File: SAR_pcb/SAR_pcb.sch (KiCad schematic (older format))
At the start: 47 parts, among them J1 Conn_Coaxial_Power, J10 Conn_Coaxial, J12 Conn_01x02, J13 Conn_01x02, J14 Conn_01x02, J15 Conn_01x02, J16 Conn_01x02, J17 Conn_01x02, J18 Conn_01x02, J19 Conn_01x02, J2 Conn_Coaxial_Power, J20 Conn_01x02, J21 Conn_01x02, J3 Conn_Coaxial_Power, J4 Conn_Coaxial_Power, J5 Conn_Coaxial_Power, J6 Conn_01x02_Male, J7 Conn_01x02_Male, J8 Conn_01x02_Male, J9 Conn_Coaxial, U2 10B_SAR

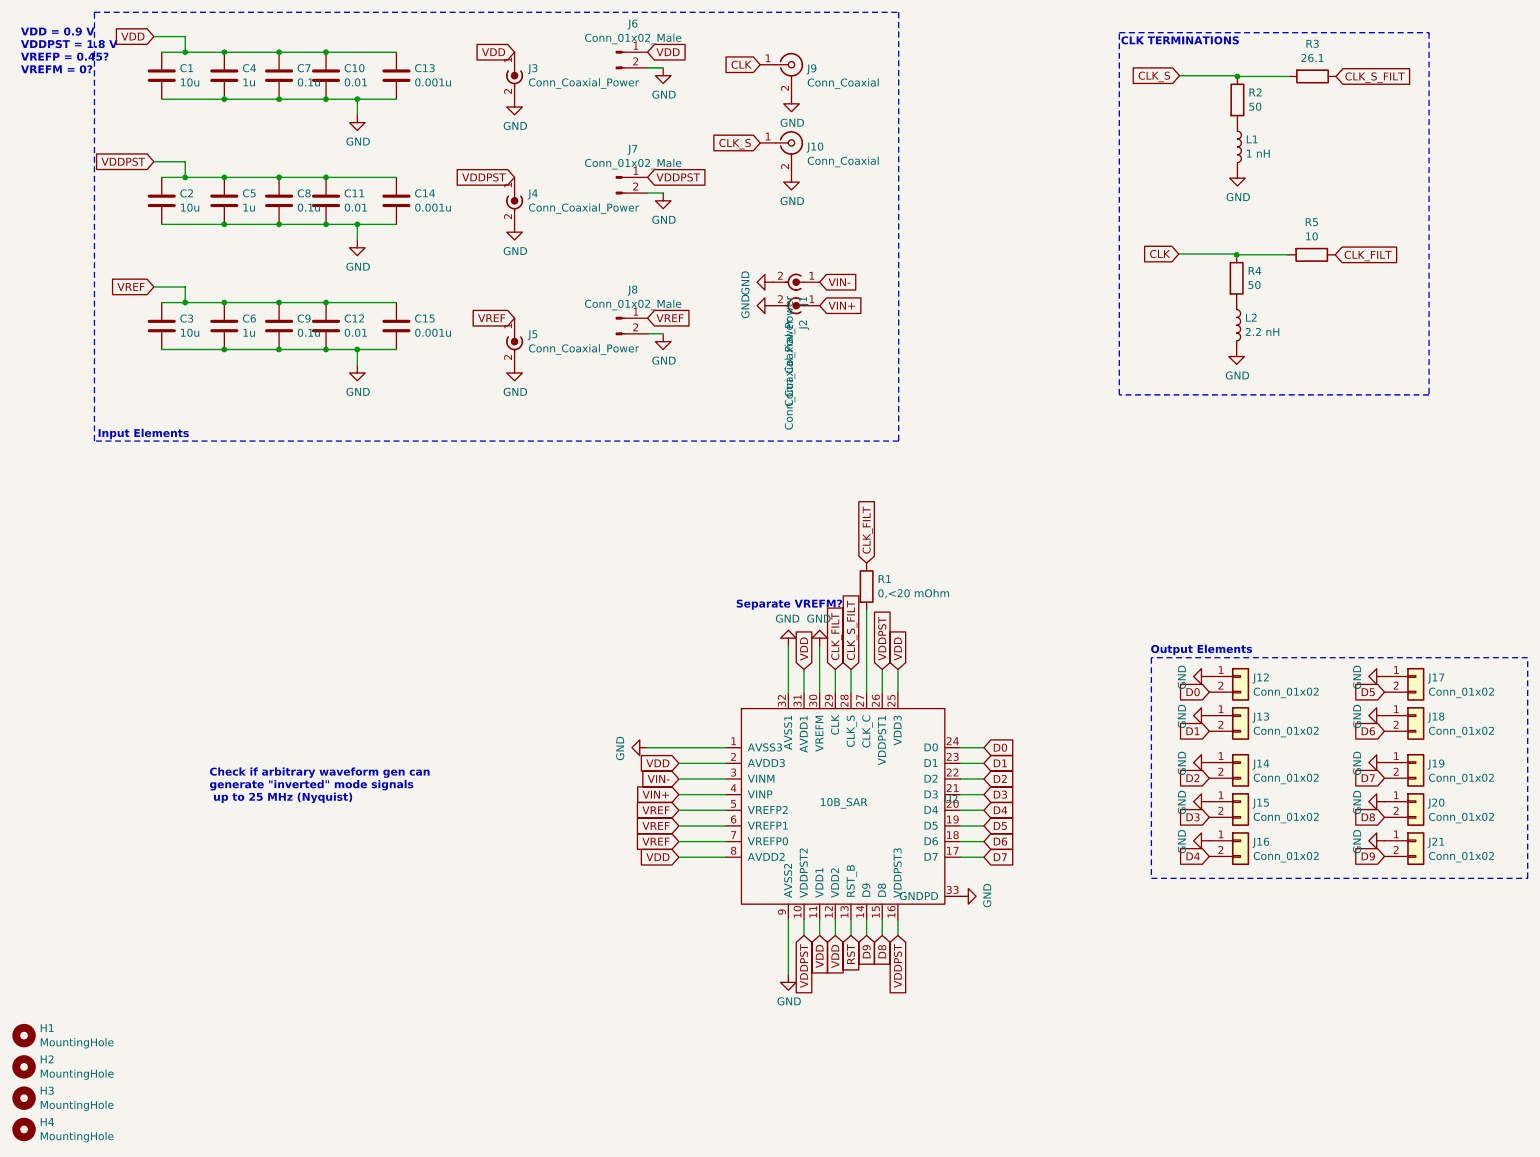
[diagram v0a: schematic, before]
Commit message: added reset switch
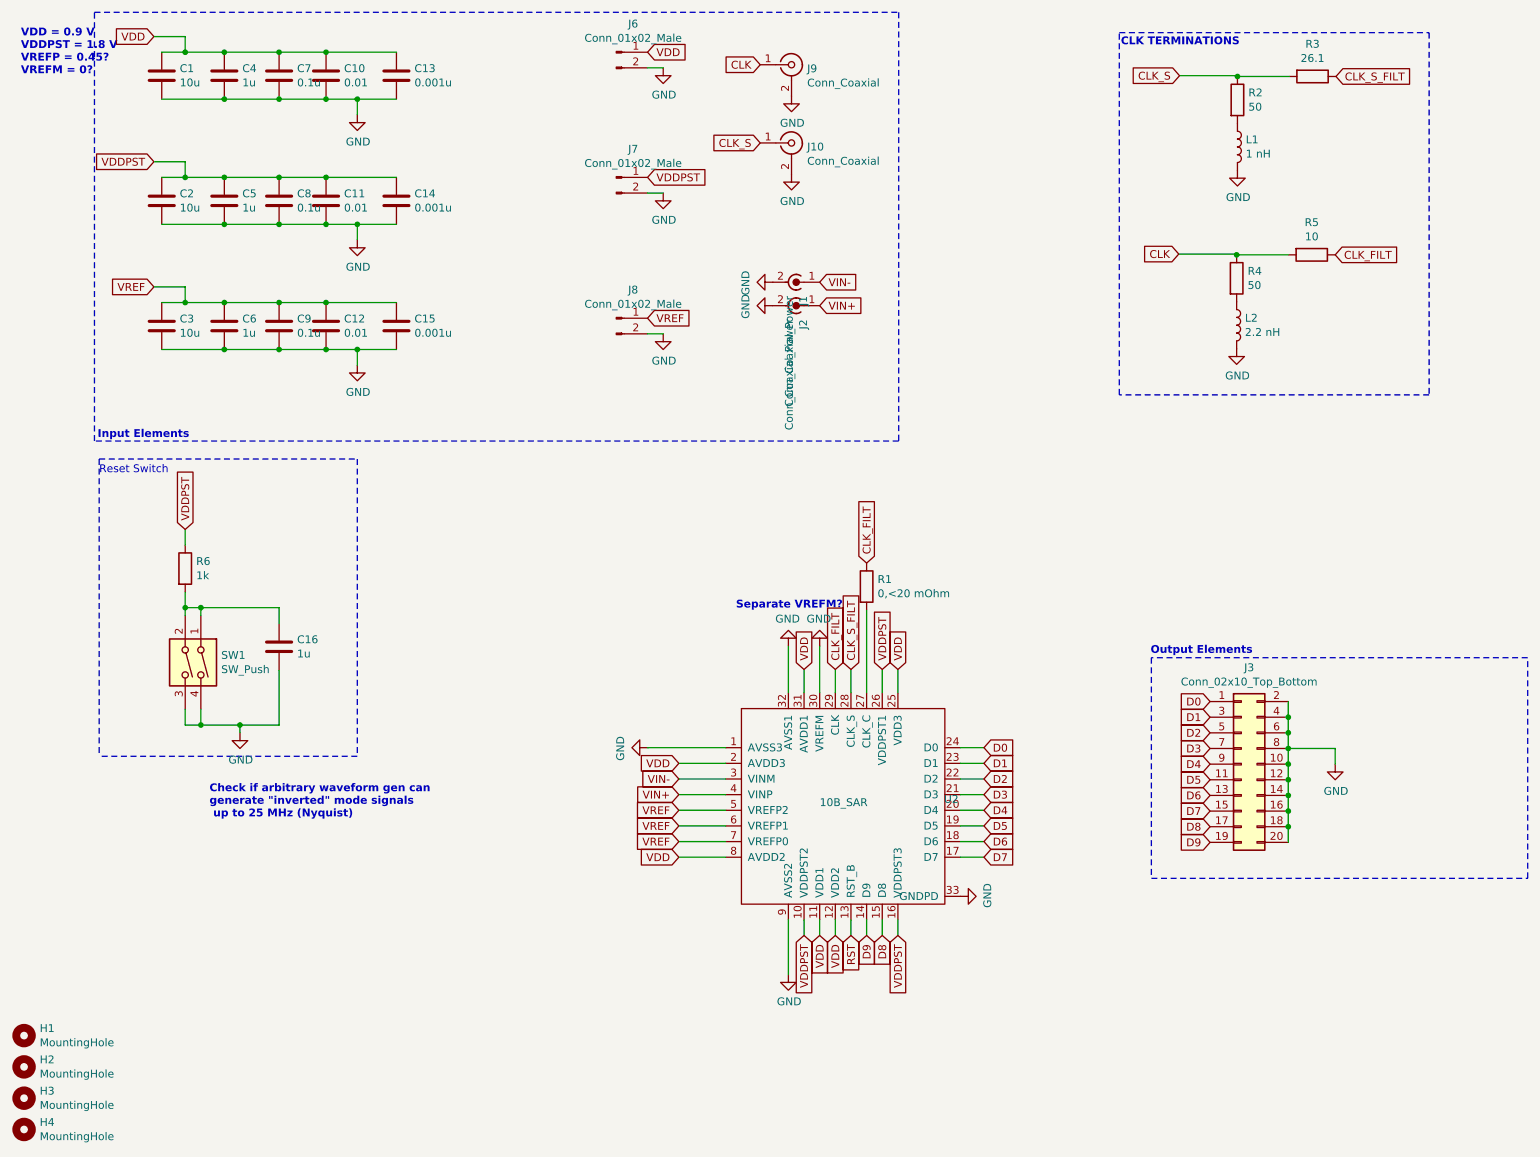
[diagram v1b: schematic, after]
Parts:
- removed J12, J13, J14, J15, J16, J17, J18, J19, J20, J21: Conn_01x02, Connector_PinHeader_2.54mm:PinHeader_1x02_P2.54mm_Vertical, symbol Connector_Generic:Conn_01x02
- removed J3, J4, J5: Conn_Coaxial_Power, Connector_Coaxial:BNC_TEConnectivity_1478204_Vertical, symbol Connector:Conn_Coaxial_Power
- added C16: 1u, Capacitor_SMD:C_0805_2012Metric, symbol Device:C
- added J3: Conn_02x10_Top_Bottom, Connector_PinHeader_2.54mm:PinHeader_2x10_P2.54mm_Vertical, symbol Connector_Generic:Conn_02x10_Odd_Even
- added R6: 1k, Resistor_SMD:R_0805_2012Metric, symbol Device:R
- added SW1: SW_Push, Button_Switch_SMD:SW_SPST_Omron_B3FS-100xP, symbol Switch:SW_DIP_x02
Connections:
- net D0: now also J3.1 (Pin_1)
- net D1: now also J3.3 (Pin_3)
- net D2: now also J3.5 (Pin_5)
- net D3: now also J3.7 (Pin_7)
- net D4: now also J3.9 (Pin_9)
- net D5: now also J3.11 (Pin_11)
- net D6: now also J3.13 (Pin_13)
- net D7: now also J3.15 (Pin_15)
- net D8: now also J3.17 (Pin_17)
- net D9: now also J3.19 (Pin_19)
- net GND: now also C16.2, J3.10 (Pin_10), J3.12 (Pin_12), J3.14 (Pin_14), J3.16 (Pin_16), J3.18 (Pin_18), J3.2 (Pin_2), J3.20 (Pin_20), J3.4 (Pin_4), J3.6 (Pin_6), J3.8 (Pin_8), SW1.3, SW1.4
- net VDDPST: now also R6.1
- new net: C16.1, R6.2, SW1.1, SW1.2
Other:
- note added: "Reset Switch\n"

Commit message: first draft of layout
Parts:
- U2: footprint Package_DFN_QFN:QFN-32-1EP_5x5mm_P0.5mm_EP3.1x3.1mm -> Package_DFN_QFN:QFN-32-1EP_5x5mm_P0.5mm_EP3.1x3.1mm_ThermalVias
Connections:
- net RST: now also C16.1, R6.2, SW1.1, SW1.2
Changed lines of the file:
@@
 F 0 "U2" H 6499 4416 50  0000 L CNN
 F 1 "10B_SAR" H 5705 4395 50  0000 L CNN
-F 2 "Package_DFN_QFN:QFN-32-1EP_5x5mm_P0.5mm_EP3.1x3.1mm" H 5805 4445 50  0001 C CNN
+F 2 "Package_DFN_QFN:QFN-32-1EP_5x5mm_P0.5mm_EP3.1x3.1mm_ThermalVias" H 5805 4445 50  0001 C CNN
 F 3 "" H 5805 4445 50  0001 C CNN
 	1    5205 4995
@@
 $EndComp
 Wire Wire Line
-	1650 4250 1650 4350
+	1650 4250 1650 4300
 $Comp
 L power:GND #PWR0102
@@
 Wire Wire Line
 	2250 4350 2250 4450
+Text GLabel 1400 4300 0    50   Input ~ 0
+RST
+Wire Wire Line
+	1400 4300 1650 4300
+Connection ~ 1650 4300
+Wire Wire Line
+	1650 4300 1650 4350
 $EndSCHEMATC

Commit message: Updated schematic to use female header pins for VDD, VDDPST, etc., finalized BOM (see BOM.csv), updated footprints
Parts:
- removed J6, J7, J8: Conn_01x02_Male, Connector_Molex:Molex_KK-254_AE-6410-02A_1x02_P2.54mm_Vertical, symbol Connector:Conn_01x02_Male
- added J4: Conn_01x06, Connector_PinSocket_2.54mm:PinSocket_1x06_P2.54mm_Vertical, symbol Connector_Generic:Conn_01x06
- SW1: footprint Button_Switch_SMD:SW_SPST_Omron_B3FS-100xP -> Button_Switch_THT:SW_DIP_SPSTx02_Slide_9.78x7.26mm_W7.62mm_P2.54mm
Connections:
- net GND: now also J4.2 (Pin_2), J4.4 (Pin_4), J4.6 (Pin_6)
- net VDD: now also J4.1 (Pin_1)
- net VDDPST: now also J4.3 (Pin_3)
- net VREF: now also J4.5 (Pin_5)
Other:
- note removed: "Check if arbitrary waveform gen can \ngenerate "inverted" mode signals\n up to 25 MHz (Nyquist)"

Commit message: Draft 2 of Layout
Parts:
- removed C10, C11, C12: 0.01, Capacitor_SMD:C_0805_2012Metric, symbol Device:C
- removed C4, C5, C6: 1u, Capacitor_SMD:C_0805_2012Metric, symbol Device:C
- removed C7, C8, C9: 0.1u, Capacitor_SMD:C_0805_2012Metric, symbol Device:C
- added C17, C18, C19, C20, C21: 0.01u, Capacitor_SMD:C_0805_2012Metric, symbol Device:C
- C13, C14, C15: value 0.001u -> 0.01u
- J10, J9: footprint Connector_Coaxial:SMA_Amphenol_132289_EdgeMount -> SAR_pcb:CustomSMA
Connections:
- net GND: now also C17.2, C18.2, C19.2, C20.2, C21.2
- net VDD: now also C17.1, C18.1, C21.1
- net VDDPST: now also C19.1, C20.1
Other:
- moved on the sheet: C13
